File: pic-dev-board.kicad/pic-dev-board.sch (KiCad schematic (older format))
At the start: 44 parts, among them J1 Conn_01x03_Male, J13 Conn_01x06_Male, J15 Barrel_Jack_Switch, J16 RUN/~PGM, J17 I2C, J18 GP1(RA1)/RB6, J19 GP2(RA2)/RB4, J2 Conn_01x03_Male, J20 Conn_01x06_Male, J3 Conn_01x03_Male, J4 Conn_01x03_Male, J5 Conn_01x03_Male, J6 Conn_01x06_Male, J7 Conn_TRISC, J8 Conn_TRISA, J9 Conn_TRISB, SW1 SW_Push, U1 PIC16F690-IP

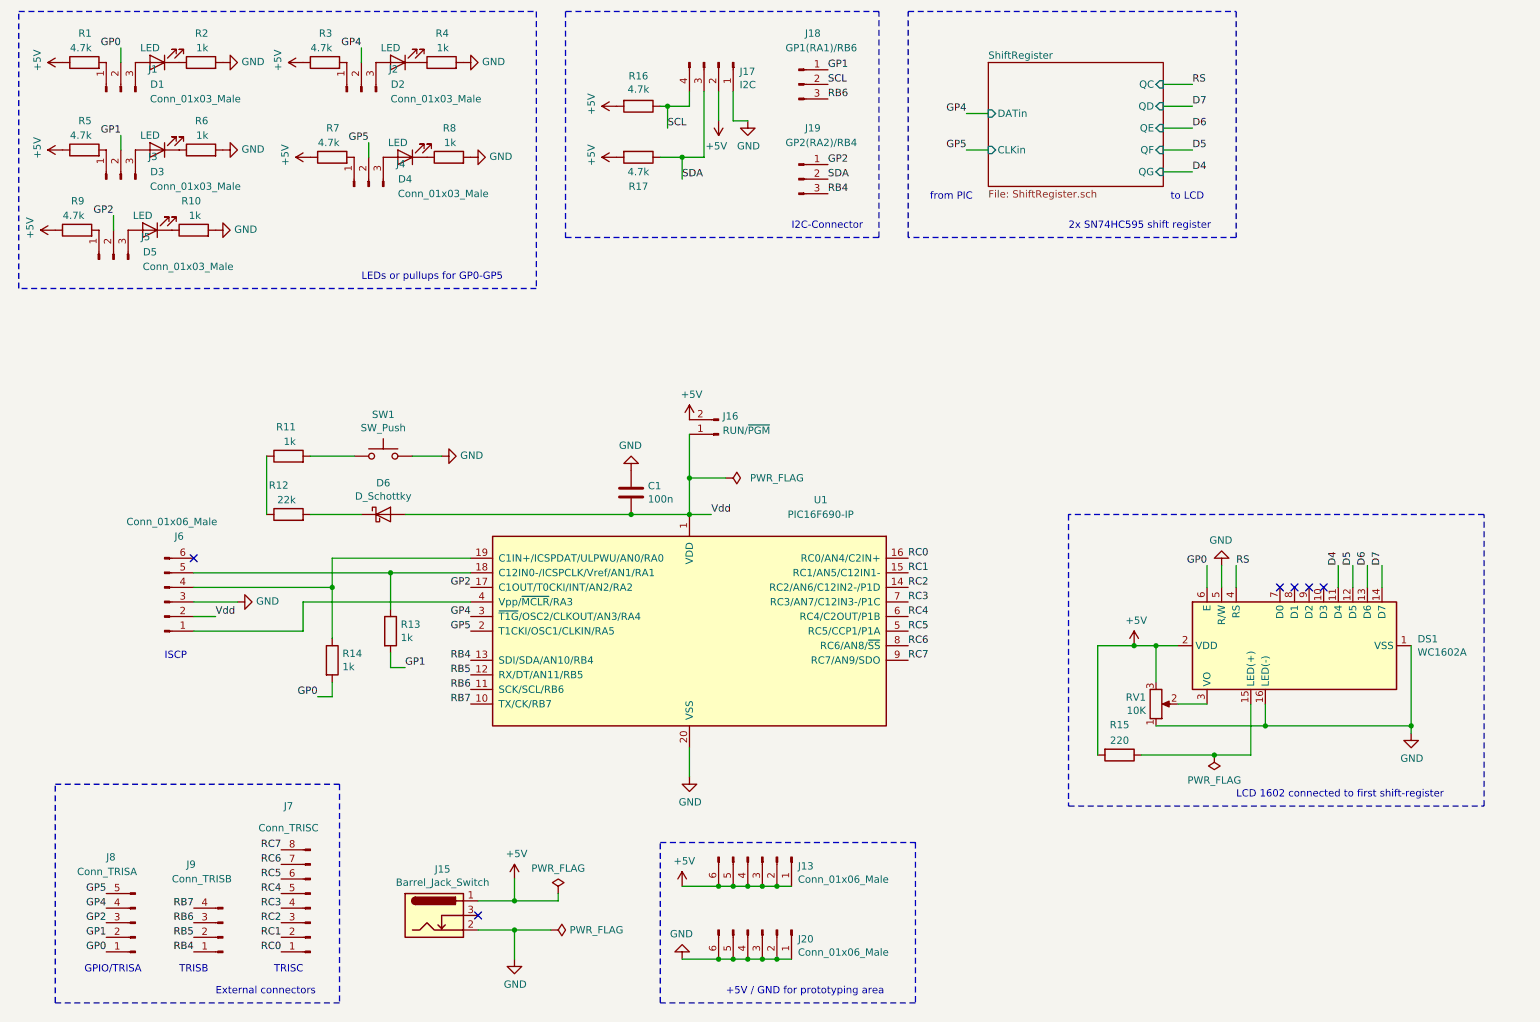
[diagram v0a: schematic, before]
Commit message: changed values of connectors
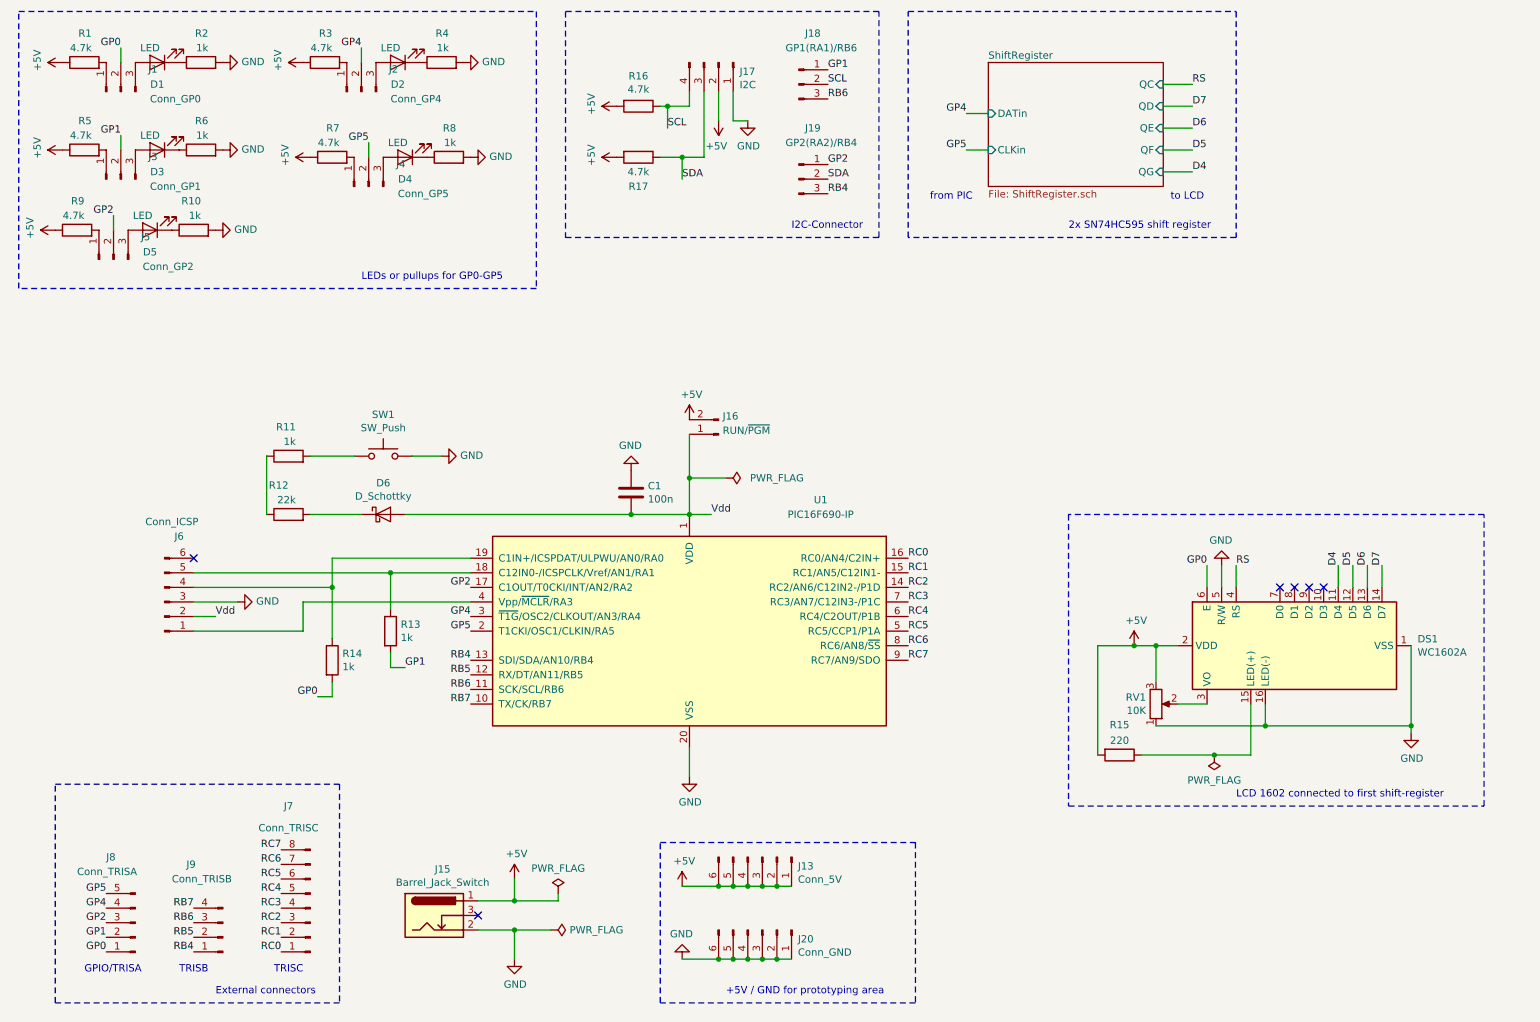
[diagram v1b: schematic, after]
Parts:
- DS1: footprint Display:WC1602A -> user:WC1602A_Connector
- J1: value Conn_01x03_Male -> Conn_GP0
- J13: value Conn_01x06_Male -> Conn_5V
- J15: footprint Connector_BarrelJack:BarrelJack_CUI_PJ-063AH_Horizontal -> Connector_BarrelJack:BarrelJack_CUI_PJ-102AH_Horizontal
- J2: value Conn_01x03_Male -> Conn_GP4
- J20: value Conn_01x06_Male -> Conn_GND
- J3: value Conn_01x03_Male -> Conn_GP1
- J4: value Conn_01x03_Male -> Conn_GP5
- J5: value Conn_01x03_Male -> Conn_GP2
- J6: value Conn_01x06_Male -> Conn_ICSP
- RV1: footprint Potentiometer_THT:Potentiometer_Vishay_T73XW_Horizontal -> Potentiometer_THT:Potentiometer_Bourns_3386X_Horizontal
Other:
- note removed: "ISCP"
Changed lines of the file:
@@
 F 0 "DS1" V 9304 4106 50  0000 R CNN
 F 1 "WC1602A" V 9395 4106 50  0000 R CNN
-F 2 "Display:WC1602A" H 9350 4050 50  0001 C CIN
+F 2 "user:WC1602A_Connector" H 9350 4050 50  0001 C CIN
 F 3 "http://www.wincomlcd.com/pdf/WC1602A-SFYLYHTC06.pdf" H 10050 4950 50  0001 C CNN
 	1    9350 4950
@@
 F 0 "RV1" H 8331 5304 50  0000 R CNN
 F 1 "10K" H 8331 5395 50  0000 R CNN
-F 2 "Potentiometer_THT:Potentiometer_Vishay_T73XW_Horizontal" H 8400 5350 50  0001 C CNN
+F 2 "Potentiometer_THT:Potentiometer_Bourns_3386X_Horizontal" H 8400 5350 50  0001 C CNN
 F 3 "~" H 8400 5350 50  0001 C CNN
 	1    8400 5350
@@
 P 1600 4650
 F 0 "J6" H 1700 4200 50  0000 C CNN
-F 1 "Conn_01x06_Male" H 1650 4100 50  0000 C CNN
+F 1 "Conn_ICSP" H 1650 4100 50  0000 C CNN
 F 2 "Connector_PinHeader_2.54mm:PinHeader_1x06_P2.54mm_Vertical" H 1600 4650 50  0001 C CNN
 F 3 "~" H 1600 4650 50  0001 C CNN
@@
 Text Label 1200 7050 2    50   ~ 0
 GP0
-Text Notes 1600 5050 0    50   ~ 0
-ISCP
 $Comp
 L Device:C C1
@@
 P 1300 1150
 F 0 "J1" V 1454 962 50  0000 R CNN
-F 1 "Conn_01x03_Male" V 1250 950 50  0000 R CNN
+F 1 "Conn_GP0" V 1250 950 50  0000 R CNN
 F 2 "Connector_PinHeader_2.54mm:PinHeader_1x03_P2.54mm_Vertical" H 1300 1150 50  0001 C CNN
 F 3 "~" H 1300 1150 50  0001 C CNN
@@
 P 2950 1150
 F 0 "J2" V 3104 962 50  0000 R CNN
-F 1 "Conn_01x03_Male" V 2900 950 50  0000 R CNN
+F 1 "Conn_GP4" V 2900 950 50  0000 R CNN
 F 2 "Connector_PinHeader_2.54mm:PinHeader_1x03_P2.54mm_Vertical" H 2950 1150 50  0001 C CNN
 F 3 "~" H 2950 1150 50  0001 C CNN
@@
 P 1300 1750
 F 0 "J3" V 1454 1562 50  0000 R CNN
-F 1 "Conn_01x03_Male" V 1250 1550 50  0000 R CNN
+F 1 "Conn_GP1" V 1250 1550 50  0000 R CNN
 F 2 "Connector_PinHeader_2.54mm:PinHeader_1x03_P2.54mm_Vertical" H 1300 1750 50  0001 C CNN
 F 3 "~" H 1300 1750 50  0001 C CNN
@@
 P 3000 1800
 F 0 "J4" V 3154 1612 50  0000 R CNN
-F 1 "Conn_01x03_Male" V 2950 1600 50  0000 R CNN
+F 1 "Conn_GP5" V 2950 1600 50  0000 R CNN
 F 2 "Connector_PinHeader_2.54mm:PinHeader_1x03_P2.54mm_Vertical" H 3000 1800 50  0001 C CNN
 F 3 "~" H 3000 1800 50  0001 C CNN
@@
 P 1250 2300
 F 0 "J5" V 1404 2112 50  0000 R CNN
-F 1 "Conn_01x03_Male" V 1200 2100 50  0000 R CNN
+F 1 "Conn_GP2" V 1200 2100 50  0000 R CNN
 F 2 "Connector_PinHeader_2.54mm:PinHeader_1x03_P2.54mm_Vertical" H 1250 2300 50  0001 C CNN
 F 3 "~" H 1250 2300 50  0001 C CNN
@@
 F 0 "J15" H 3507 7117 50  0000 C CNN
 F 1 "Barrel_Jack_Switch" H 3507 7026 50  0000 C CNN
-F 2 "Connector_BarrelJack:BarrelJack_CUI_PJ-063AH_Horizontal" H 3500 6760 50  0001 C CNN
+F 2 "Connector_BarrelJack:BarrelJack_CUI_PJ-102AH_Horizontal" H 3500 6760 50  0001 C CNN
 F 3 "~" H 3500 6760 50  0001 C CNN
 	1    3450 6800
@@
 P 5700 6400
 F 0 "J13" V 5762 6644 50  0000 L CNN
-F 1 "Conn_01x06_Male" V 5853 6644 50  0000 L CNN
+F 1 "Conn_5V" V 5853 6644 50  0000 L CNN
 F 2 "Connector_PinHeader_2.54mm:PinHeader_1x06_P2.54mm_Vertical" H 5700 6400 50  0001 C CNN
 F 3 "~" H 5700 6400 50  0001 C CNN
@@
 P 5700 6900
 F 0 "J20" V 5762 7144 50  0000 L CNN
-F 1 "Conn_01x06_Male" V 5853 7144 50  0000 L CNN
+F 1 "Conn_GND" V 5853 7144 50  0000 L CNN
 F 2 "Connector_PinHeader_2.54mm:PinHeader_1x06_P2.54mm_Vertical" H 5700 6900 50  0001 C CNN
 F 3 "~" H 5700 6900 50  0001 C CNN

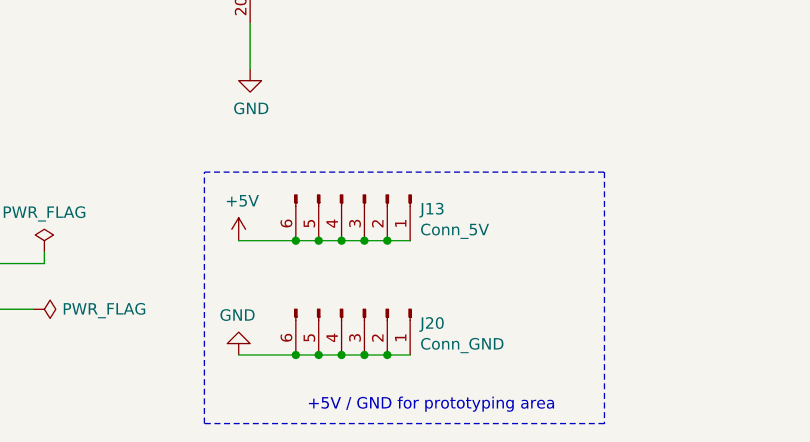
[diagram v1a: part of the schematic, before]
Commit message: changed +5V/GND connector
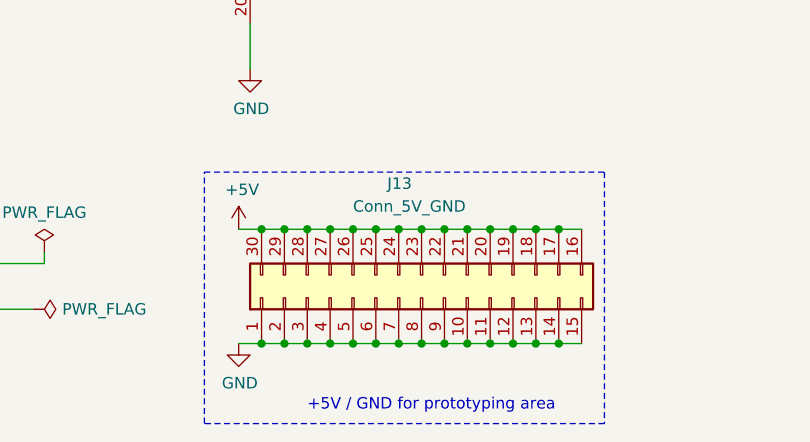
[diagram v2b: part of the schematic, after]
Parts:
- removed J13: Conn_5V, Connector_PinHeader_2.54mm:PinHeader_1x06_P2.54mm_Vertical, symbol Connector:Conn_01x06_Male
- removed J20: Conn_GND, Connector_PinHeader_2.54mm:PinHeader_1x06_P2.54mm_Vertical, symbol Connector:Conn_01x06_Male
- added J13: Conn_5V_GND, Connector_PinHeader_2.54mm:PinHeader_2x15_P2.54mm_Vertical, symbol Connector_Generic:Conn_02x15_Counter_Clockwise
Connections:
- net +5V: now also J13.16 (Pin_16), J13.17 (Pin_17), J13.18 (Pin_18), J13.19 (Pin_19), J13.20 (Pin_20), J13.21 (Pin_21), J13.22 (Pin_22), J13.23 (Pin_23), J13.24 (Pin_24), J13.25 (Pin_25), J13.26 (Pin_26), J13.27 (Pin_27), J13.28 (Pin_28), J13.29 (Pin_29), J13.30 (Pin_30)
- net GND: now also J13.1 (Pin_1), J13.10 (Pin_10), J13.11 (Pin_11), J13.12 (Pin_12), J13.13 (Pin_13), J13.14 (Pin_14), J13.15 (Pin_15), J13.2 (Pin_2), J13.3 (Pin_3), J13.4 (Pin_4), J13.5 (Pin_5), J13.6 (Pin_6), J13.7 (Pin_7), J13.8 (Pin_8), J13.9 (Pin_9)
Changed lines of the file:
@@
 Sheet 1 2
 Title "PIC Development Board"
-Date "2020-08-13"
+Date "2020-08-17"
 Rev "1"
 Comp "Bernhard Bablok"
@@
 Text Notes 8500 1900 0    50   ~ 0
 to LCD
-$Comp
-L Connector:Conn_01x06_Male J13
-U 1 1 5F40173F
-P 5700 6400
-F 0 "J13" V 5762 6644 50  0000 L CNN
-F 1 "Conn_5V" V 5853 6644 50  0000 L CNN
-F 2 "Connector_PinHeader_2.54mm:PinHeader_1x06_P2.54mm_Vertical" H 5700 6400 50  0001 C CNN
-F 3 "~" H 5700 6400 50  0001 C CNN
-	1    5700 6400
-	0    1    1    0
-$EndComp
-$Comp
-L Connector:Conn_01x06_Male J20
-U 1 1 5F402982
-P 5700 6900
-F 0 "J20" V 5762 7144 50  0000 L CNN
-F 1 "Conn_GND" V 5853 7144 50  0000 L CNN
-F 2 "Connector_PinHeader_2.54mm:PinHeader_1x06_P2.54mm_Vertical" H 5700 6900 50  0001 C CNN
-F 3 "~" H 5700 6900 50  0001 C CNN
-	1    5700 6900
-	0    1    1    0
-$EndComp
-$Comp
-L power:+5V #PWR028
-U 1 1 5F403557
-P 5150 6600
-F 0 "#PWR028" H 5150 6450 50  0001 C CNN
-F 1 "+5V" H 5165 6773 50  0000 C CNN
-F 2 "" H 5150 6600 50  0001 C CNN
-F 3 "" H 5150 6600 50  0001 C CNN
-	1    5150 6600
-	1    0    0    -1
-$EndComp
-$Comp
-L power:GND #PWR029
-U 1 1 5F403BD0
-P 5150 7100
-F 0 "#PWR029" H 5150 6850 50  0001 C CNN
-F 1 "GND" H 5155 6927 50  0000 C CNN
-F 2 "" H 5150 7100 50  0001 C CNN
-F 3 "" H 5150 7100 50  0001 C CNN
-	1    5150 7100
-	-1   0    0    1
-$EndComp
-Wire Wire Line
-	5150 6600 5400 6600
-Connection ~ 5400 6600
-Wire Wire Line
-	5400 6600 5500 6600
-Connection ~ 5500 6600
-Wire Wire Line
-	5500 6600 5600 6600
-Connection ~ 5600 6600
-Wire Wire Line
-	5600 6600 5700 6600
-Connection ~ 5700 6600
-Wire Wire Line
-	5700 6600 5800 6600
-Connection ~ 5800 6600
-Wire Wire Line
-	5800 6600 5900 6600
-Wire Wire Line
-	5150 7100 5400 7100
-Connection ~ 5400 7100
-Wire Wire Line
-	5400 7100 5500 7100
-Connection ~ 5500 7100
-Wire Wire Line
-	5500 7100 5600 7100
-Connection ~ 5600 7100
-Wire Wire Line
-	5600 7100 5700 7100
-Connection ~ 5700 7100
-Wire Wire Line
-	5700 7100 5800 7100
-Connection ~ 5800 7100
-Wire Wire Line
-	5800 7100 5900 7100
 Wire Notes Line
 	5000 6300 6750 6300
@@
 Text Notes 7800 2100 0    50   ~ 0
 2x SN74HC595 shift register
+$Comp
+L Connector_Generic:Conn_02x15_Counter_Clockwise J13
+U 1 1 5F3C7703
+P 5950 6850
+F 0 "J13" V 6450 7000 50  0000 R CNN
+F 1 "Conn_5V_GND" V 6350 7150 50  0000 R CNN
+F 2 "Connector_PinHeader_2.54mm:PinHeader_2x15_P2.54mm_Vertical" H 5950 6850 50  0001 C CNN
+F 3 "~" H 5950 6850 50  0001 C CNN
+	1    5950 6850
+	0    -1   -1   0
+$EndComp
+$Comp
+L power:GND #PWR029
+U 1 1 5F3CE45A
+P 5150 7050
+F 0 "#PWR029" H 5150 6800 50  0001 C CNN
+F 1 "GND" H 5155 6877 50  0000 C CNN
+F 2 "" H 5150 7050 50  0001 C CNN
+F 3 "" H 5150 7050 50  0001 C CNN
+	1    5150 7050
+	1    0    0    -1
+$EndComp
+$Comp
+L power:+5V #PWR028
+U 1 1 5F3CEC58
+P 5150 6550
+F 0 "#PWR028" H 5150 6400 50  0001 C CNN
+F 1 "+5V" H 5165 6723 50  0000 C CNN
+F 2 "" H 5150 6550 50  0001 C CNN
+F 3 "" H 5150 6550 50  0001 C CNN
+	1    5150 6550
+	1    0    0    -1
+$EndComp
+Wire Wire Line
+	5150 6550 5250 6550
+Connection ~ 5250 6550
+Wire Wire Line
+	5250 6550 5350 6550
+Connection ~ 5350 6550
+Wire Wire Line
+	5350 6550 5450 6550
+Connection ~ 5450 6550
+Wire Wire Line
+	5450 6550 5550 6550
+Connection ~ 5550 6550
+Wire Wire Line
+	5550 6550 5650 6550
+Connection ~ 5650 6550
+Wire Wire Line
+	5650 6550 5750 6550
+Connection ~ 5750 6550
+Wire Wire Line
+	5750 6550 5850 6550
+Connection ~ 5850 6550
+Wire Wire Line
+	5850 6550 5950 6550
+Connection ~ 5950 6550
+Wire Wire Line
+	5950 6550 6050 6550
+Connection ~ 6050 6550
+Wire Wire Line
+	6050 6550 6150 6550
+Connection ~ 6150 6550
+Wire Wire Line
+	6150 6550 6250 6550
+Connection ~ 6250 6550
+Wire Wire Line
+	6250 6550 6350 6550
+Connection ~ 6350 6550
+Wire Wire Line
+	6350 6550 6450 6550
+Connection ~ 6450 6550
+Wire Wire Line
+	6450 6550 6550 6550
+Connection ~ 6550 6550
+Wire Wire Line
+	6550 6550 6650 6550
+Wire Wire Line
+	6650 7050 6550 7050
+Connection ~ 5250 7050
+Wire Wire Line
+	5250 7050 5150 7050
+Connection ~ 5350 7050
+Wire Wire Line
+	5350 7050 5250 7050
+Connection ~ 5450 7050
+Wire Wire Line
+	5450 7050 5350 7050
+Connection ~ 5550 7050
+Wire Wire Line
+	5550 7050 5450 7050
+Connection ~ 5650 7050
+Wire Wire Line
+	5650 7050 5550 7050
+Connection ~ 5750 7050
+Wire Wire Line
+	5750 7050 5650 7050
+Connection ~ 5850 7050
+Wire Wire Line
+	5850 7050 5750 7050
+Connection ~ 5950 7050
+Wire Wire Line
+	5950 7050 5850 7050
+Connection ~ 6050 7050
+Wire Wire Line
+	6050 7050 5950 7050
+Connection ~ 6150 7050
+Wire Wire Line
+	6150 7050 6050 7050
+Connection ~ 6250 7050
+Wire Wire Line
+	6250 7050 6150 7050
+Connection ~ 6350 7050
+Wire Wire Line
+	6350 7050 6250 7050
+Connection ~ 6450 7050
+Wire Wire Line
+	6450 7050 6350 7050
+Connection ~ 6550 7050
+Wire Wire Line
+	6550 7050 6450 7050
 $EndSCHEMATC
